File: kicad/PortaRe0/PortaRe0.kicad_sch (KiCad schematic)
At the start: 0 parts

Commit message: Add project docs and complete BQ25895 schematic
- Add Claude/ folder (CONTEXT.md, PROGRESS.md, PROJECT_PLAN.md, chat_logs/)
- Add KiCad hierarchical sheets (power, usb_hub, keyboard, audio)
- Complete BQ25895 power sheet schematic
  - TS pin: REGN-R6(10kΩ)-TS-R7(10kΩ)-GND divider
  - BAT/SYS/PGND/PAD/SW/BTST/REGN/PMID/DSEL all connected
  - Decoupling caps on VBAT and VSYS

Co-Authored-By: Claude Sonnet 4.6 <noreply@anthropic.com>
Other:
- added sheet audio (audio.kicad_sch)
- added sheet keyboard (keyboard.kicad_sch)
- added sheet power (power.kicad_sch)
- added sheet usb_hub (usb_hub.kicad_sch)
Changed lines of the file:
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@@
 	(generator_version "9.0")
 	(paper "A4")
+	(sheet
+		(at 16.51 96.52)
+		(size 90.17 88.9)
+		(exclude_from_sim no)
+		(in_bom yes)
+		(on_board yes)
+		(dnp no)
+		(fields_autoplaced yes)
+		(stroke
+			(width 0.1524)
+			(type solid)
+		)
+		(fill
+			(color 0 0 0 0.0000)
+		)
+		(property "Sheetname" "keyboard"
+			(at 16.51 95.8084 0)
+			(effects
+				(font
+					(size 1.27 1.27)
+				)
+				(justify left bottom)
+			)
+		)
+		(property "Sheetfile" "keyboard.kicad_sch"
+			(at 16.51 186.0046 0)
+			(effects
+				(font
+					(size 1.27 1.27)
+				)
+				(justify left top)
+			)
+		)
+		(instances
+			(project "PortaRe0"
+				(path "/479aadc4-f9a0-4ec2-b000-6a17237038f1"
+					(page "4")
+				)
+			)
+		)
+	)
+	(sheet
+		(at 107.95 96.52)
+		(size 90.17 88.9)
+		(exclude_from_sim no)
+		(in_bom yes)
+		(on_board yes)
+		(dnp no)
+		(fields_autoplaced yes)
+		(stroke
+			(width 0.1524)
+			(type solid)
+		)
+		(fill
+			(color 0 0 0 0.0000)
+		)
+		(property "Sheetname" "audio"
+			(at 107.95 95.8084 0)
+			(effects
+				(font
+					(size 1.27 1.27)
+				)
+				(justify left bottom)
+			)
+		)
+		(property "Sheetfile" "audio.kicad_sch"
+			(at 107.95 186.0046 0)
+			(effects
+				(font
+					(size 1.27 1.27)
+				)
+				(justify left top)
+			)
+		)
+		(instances
+			(project "PortaRe0"
+				(path "/479aadc4-f9a0-4ec2-b000-6a17237038f1"
+					(page "5")
+				)
+			)
+		)
+	)
+	(sheet
+		(at 107.95 17.78)
+		(size 90.17 77.47)
+		(exclude_from_sim no)
+		(in_bom yes)
+		(on_board yes)
+		(dnp no)
+		(fields_autoplaced yes)
+		(stroke
+			(width 0.1524)
+			(type solid)
+		)
+		(fill
+			(color 0 0 0 0.0000)
+		)
+		(property "Sheetname" "usb_hub"
+			(at 107.95 17.0684 0)
+			(effects
+				(font
+					(size 1.27 1.27)
+				)
+				(justify left bottom)
+			)
+		)
+		(property "Sheetfile" "usb_hub.kicad_sch"
+			(at 107.95 95.8346 0)
+			(effects
+				(font
+					(size 1.27 1.27)
+				)
+				(justify left top)
+			)
+		)
+		(instances
+			(project "PortaRe0"
+				(path "/479aadc4-f9a0-4ec2-b000-6a17237038f1"
+					(page "3")
+				)
+			)
+		)
+	)
+	(sheet
+		(at 16.51 17.78)
+		(size 90.17 77.47)
+		(exclude_from_sim no)
+		(in_bom yes)
+		(on_board yes)
+		(dnp no)
+		(fields_autoplaced yes)
+		(stroke
+			(width 0.1524)
+			(type solid)
+		)
+		(fill
+			(color 0 0 0 0.0000)
+		)
+		(property "Sheetname" "power"
+			(at 16.51 17.0684 0)
+			(effects
+				(font
+					(size 1.27 1.27)
+				)
+				(justify left bottom)
+			)
+		)
+		(property "Sheetfile" "power.kicad_sch"
+			(at 16.51 95.8346 0)
+			(effects
+				(font
+					(size 1.27 1.27)
+				)
+				(justify left top)
+			)
+		)
+		(instances
+			(project "PortaRe0"
+				(path "/479aadc4-f9a0-4ec2-b000-6a17237038f1"
+					(page "2")
+				)
+			)
+		)
+	)
 	(sheet_instances
 		(path "/"

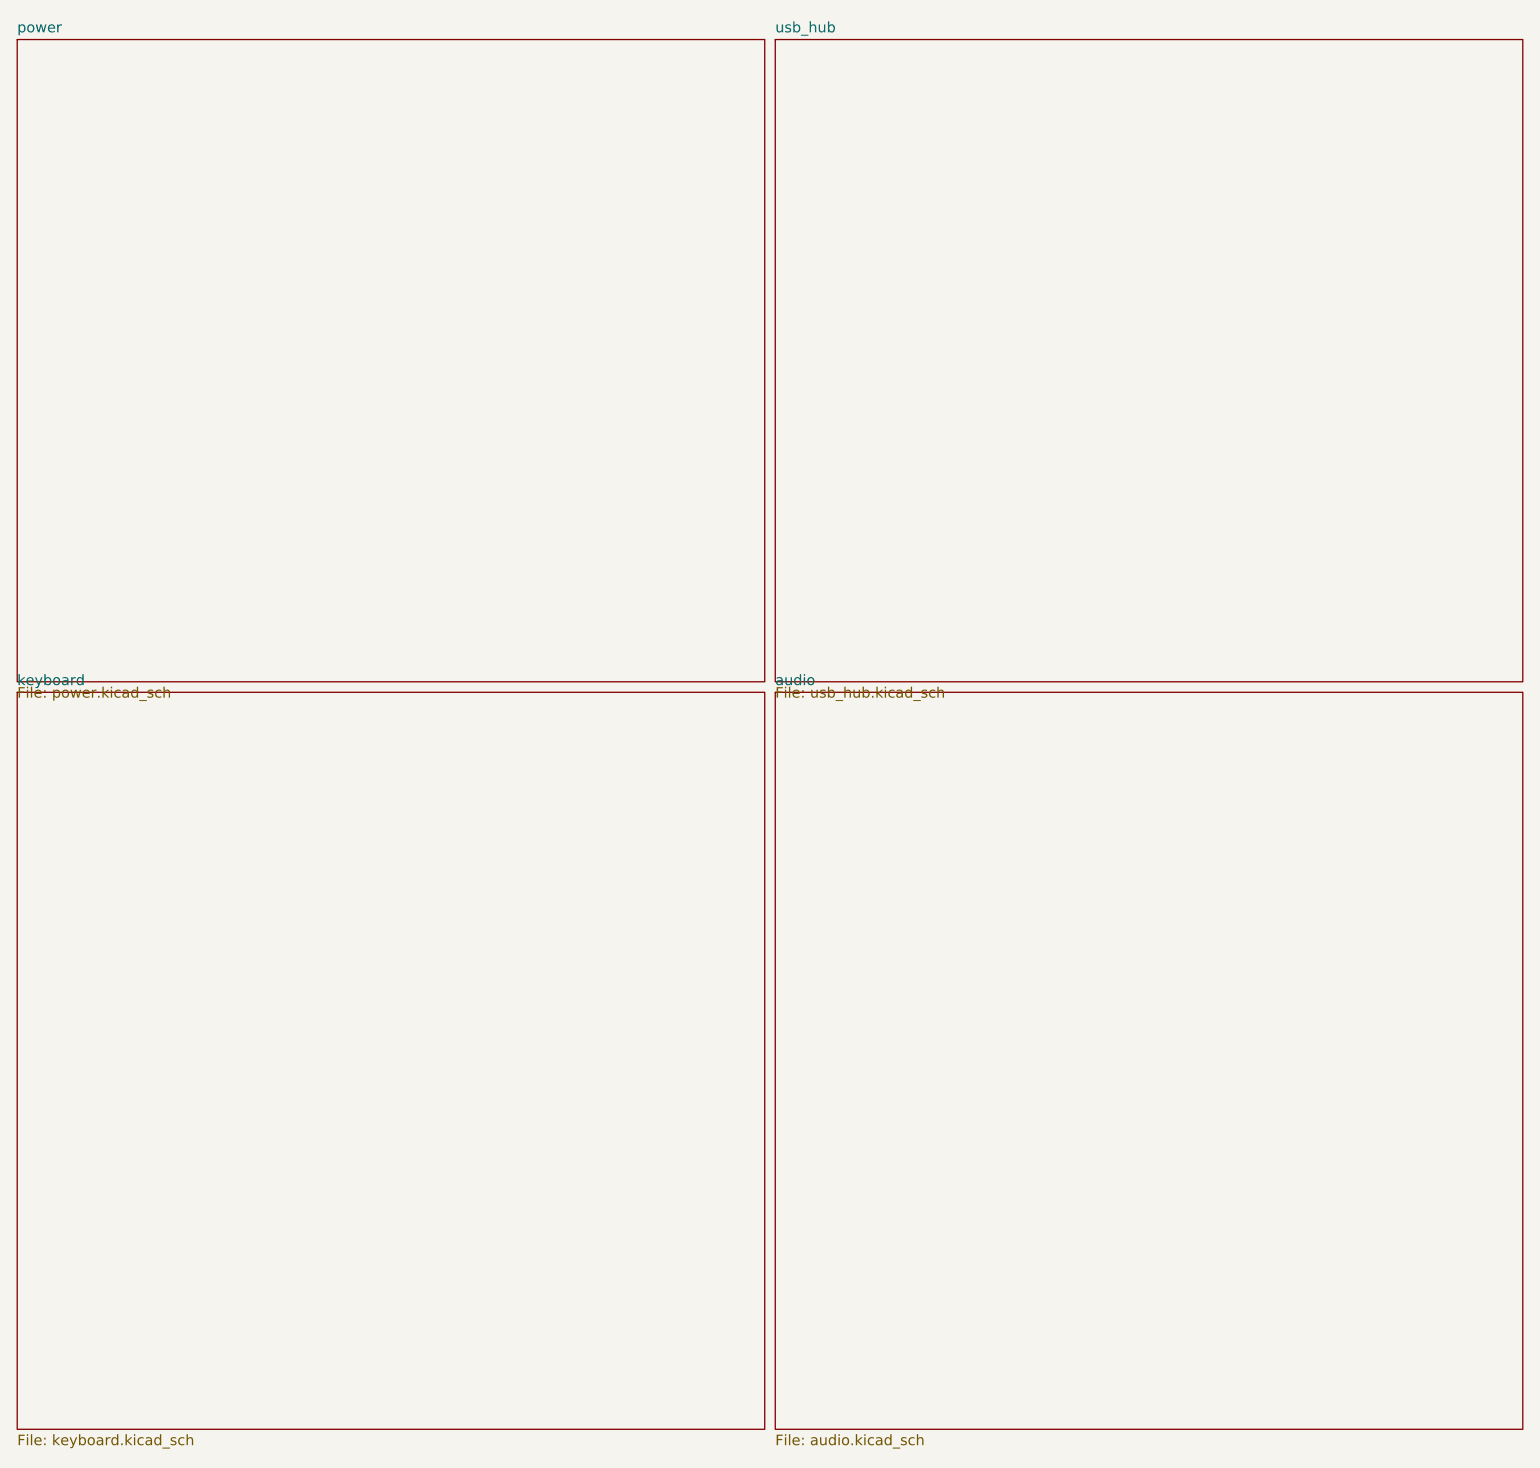
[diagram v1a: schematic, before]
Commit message: session07: キーレイアウト確定・GPIO割り当て・power回路レビュー
- キーレイアウト確定（66キー / 9×8マトリクス）、keyboard-layout.json追加
- RP2040 GPIO割り当て確定（29本/30本）をPROJECT_PLANに追記
- power回路レビュー（5V_SYS→パワーシンボル化、SCL/SDA/USB_DP/USB_DM→GlobalLabel）
- .gitignoreに.claude/を追加

Co-Authored-By: Claude Sonnet 4.6 <noreply@anthropic.com>
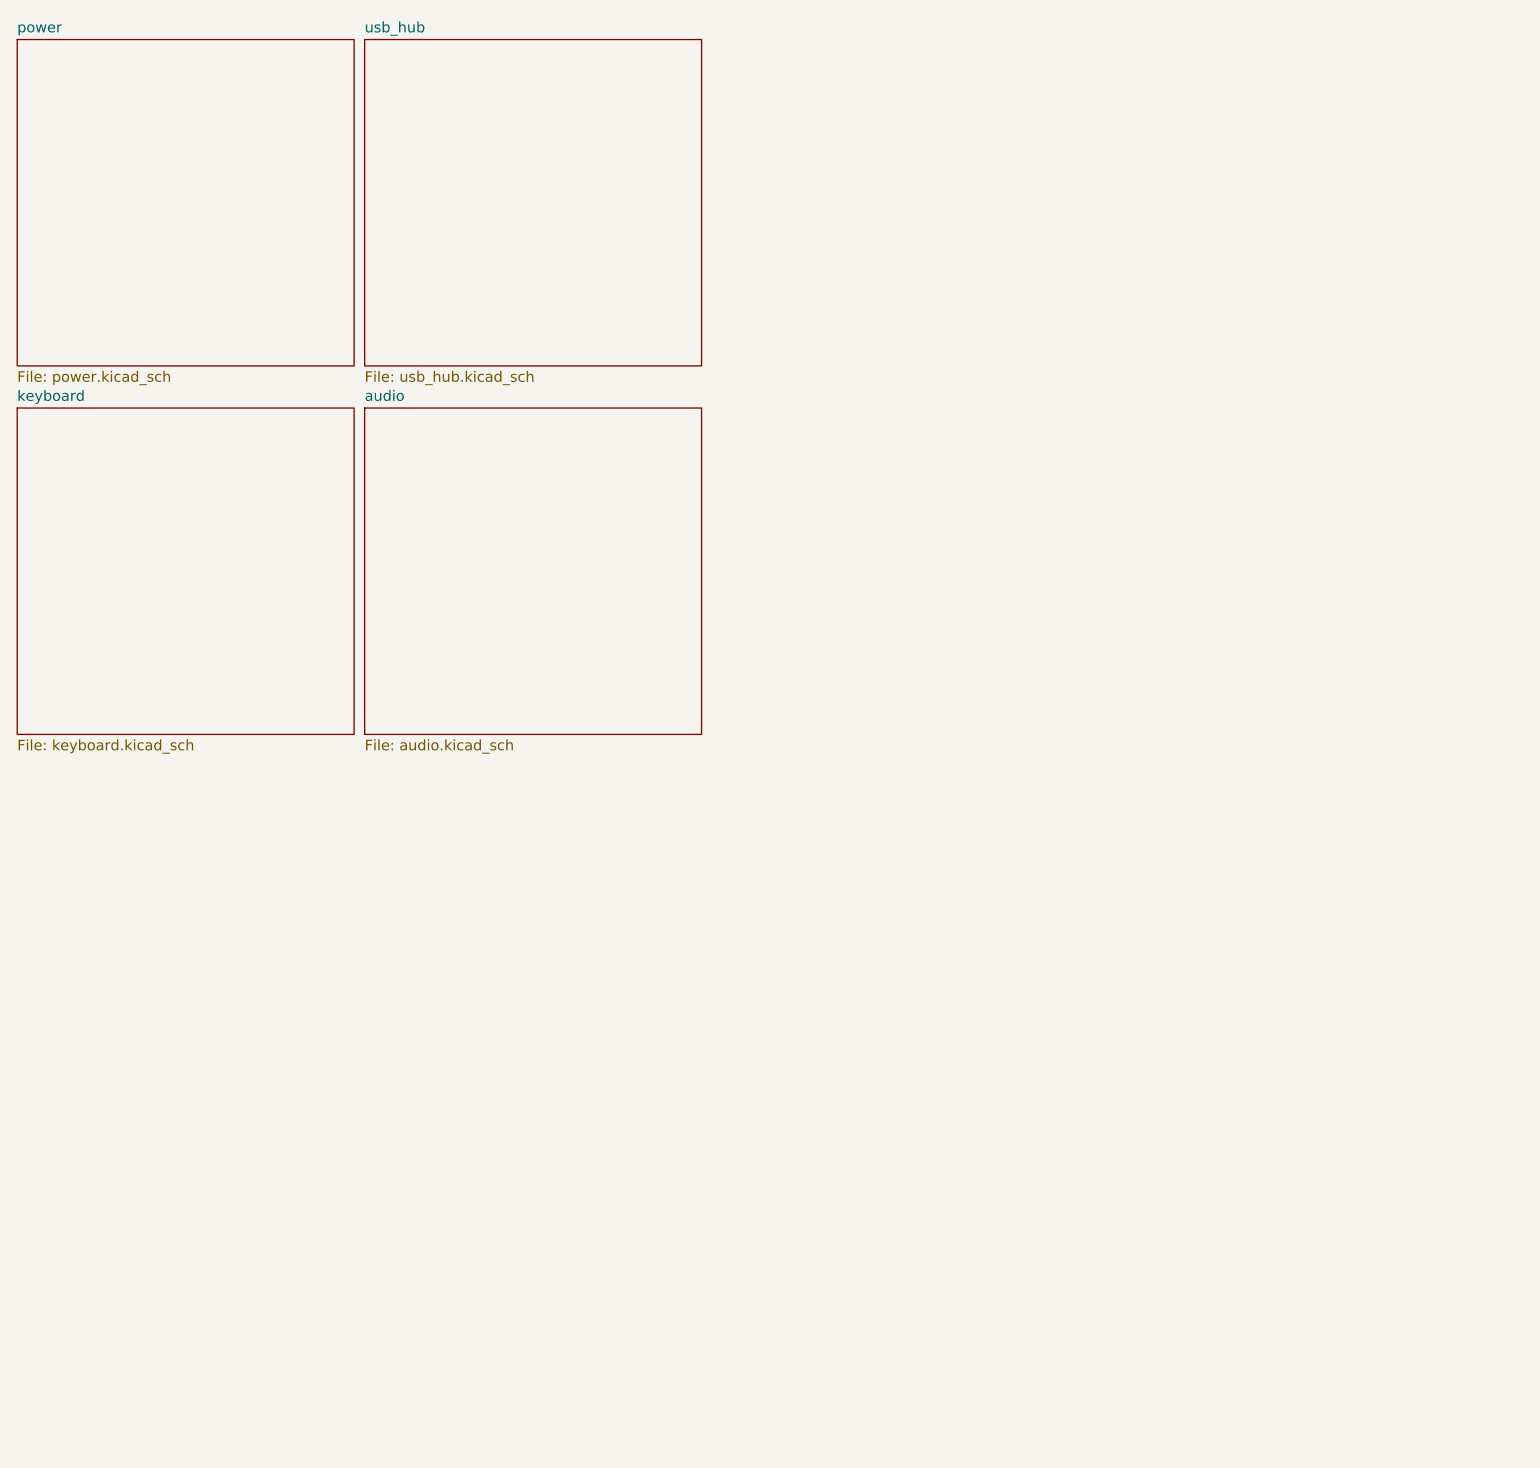
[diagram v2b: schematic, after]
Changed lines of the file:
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@@
 	(paper "A4")
 	(sheet
-		(at 16.51 96.52)
-		(size 90.17 88.9)
+		(at 16.51 62.23)
+		(size 40.64 39.37)
 		(exclude_from_sim no)
 		(in_bom yes)
@@
 		)
 		(property "Sheetname" "keyboard"
-			(at 16.51 95.8084 0)
+			(at 16.51 61.5184 0)
 			(effects
 				(font
@@
 		)
 		(property "Sheetfile" "keyboard.kicad_sch"
-			(at 16.51 186.0046 0)
+			(at 16.51 102.1846 0)
 			(effects
 				(font
@@
 	)
 	(sheet
-		(at 107.95 96.52)
-		(size 90.17 88.9)
+		(at 58.42 62.23)
+		(size 40.64 39.37)
 		(exclude_from_sim no)
 		(in_bom yes)
@@
 		)
 		(property "Sheetname" "audio"
-			(at 107.95 95.8084 0)
+			(at 58.42 61.5184 0)
 			(effects
 				(font
@@
 		)
 		(property "Sheetfile" "audio.kicad_sch"
-			(at 107.95 186.0046 0)
+			(at 58.42 102.1846 0)
 			(effects
 				(font
@@
 	)
 	(sheet
-		(at 107.95 17.78)
-		(size 90.17 77.47)
+		(at 58.42 17.78)
+		(size 40.64 39.37)
 		(exclude_from_sim no)
 		(in_bom yes)
@@
 		)
 		(property "Sheetname" "usb_hub"
-			(at 107.95 17.0684 0)
+			(at 58.42 17.0684 0)
 			(effects
 				(font
@@
 		)
 		(property "Sheetfile" "usb_hub.kicad_sch"
-			(at 107.95 95.8346 0)
+			(at 58.42 57.7346 0)
 			(effects
 				(font
@@
 	(sheet
 		(at 16.51 17.78)
-		(size 90.17 77.47)
+		(size 40.64 39.37)
 		(exclude_from_sim no)
 		(in_bom yes)
@@
 		)
 		(property "Sheetfile" "power.kicad_sch"
-			(at 16.51 95.8346 0)
+			(at 16.51 57.7346 0)
 			(effects
 				(font

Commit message: Docs: session18終了処理・PROGRESS/index更新・connectorsシート設計方針確定
- J_HDMI_CTRL: 24pin FPC 0.5mm (C2856805) ライブラリ取得・配置方針確定
- SBC接続: サブ基板→FPCに変更・スティフナーにMicro HDMIオス+USB-Cオス直付け方針
- connectors.kicad_sch 追加

Co-Authored-By: Claude Sonnet 4.6 <noreply@anthropic.com>
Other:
- added sheet Connectors (Connectors.kicad_sch)
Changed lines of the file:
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@@
 	(paper "A4")
+	(sheet
+		(at 101.6 17.78)
+		(size 39.37 39.37)
+		(exclude_from_sim no)
+		(in_bom yes)
+		(on_board yes)
+		(dnp no)
+		(fields_autoplaced yes)
+		(stroke
+			(width 0.1524)
+			(type solid)
+		)
+		(fill
+			(color 0 0 0 0.0000)
+		)
+		(property "Sheetname" "Connectors"
+			(at 101.6 17.0684 0)
+			(effects
+				(font
+					(size 1.27 1.27)
+				)
+				(justify left bottom)
+			)
+		)
+		(property "Sheetfile" "Connectors.kicad_sch"
+			(at 101.6 57.7346 0)
+			(effects
+				(font
+					(size 1.27 1.27)
+				)
+				(justify left top)
+			)
+		)
+		(instances
+			(project "PortaRe0"
+				(path "/479aadc4-f9a0-4ec2-b000-6a17237038f1"
+					(page "7")
+				)
+			)
+		)
+	)
 	(sheet
 		(at 16.51 62.23)

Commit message: Docs: session21終了処理・PROGRESS/index更新・connectorsシート完成・ERC対処
- connectors シート完成（J_SBC_HDMI / J_FAN配置完了）
- hdmi_adapter シート新設（別基板 / J_MICROHDMI Conn_02x08 + C2856805）
- J_FAN: F16FB選定（16×16×4.5mm 5V）/ BSS138回路 / FAN_PWM GlobalLabel
- 全シートERC実施・対処完了（VL812未接続ピン / SWD NC / DC10FB追加等）

Co-Authored-By: Claude Sonnet 4.6 <noreply@anthropic.com>
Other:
- added sheet hdmi_adapter (hdmi_adapter.kicad_sch)
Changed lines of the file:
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@@
 	(paper "A4")
+	(sheet
+		(at 101.6 62.23)
+		(size 39.37 39.37)
+		(exclude_from_sim no)
+		(in_bom yes)
+		(on_board yes)
+		(dnp no)
+		(fields_autoplaced yes)
+		(stroke
+			(width 0.1524)
+			(type solid)
+		)
+		(fill
+			(color 0 0 0 0.0000)
+		)
+		(property "Sheetname" "hdmi_adapter"
+			(at 101.6 61.5184 0)
+			(effects
+				(font
+					(size 1.27 1.27)
+				)
+				(justify left bottom)
+			)
+		)
+		(property "Sheetfile" "hdmi_adapter.kicad_sch"
+			(at 101.6 102.1846 0)
+			(effects
+				(font
+					(size 1.27 1.27)
+				)
+				(justify left top)
+			)
+		)
+		(instances
+			(project "PortaRe0"
+				(path "/479aadc4-f9a0-4ec2-b000-6a17237038f1"
+					(page "7")
+				)
+			)
+		)
+	)
 	(sheet
 		(at 101.6 17.78)
@@
 			(project "PortaRe0"
 				(path "/479aadc4-f9a0-4ec2-b000-6a17237038f1"
-					(page "7")
+					(page "6")
 				)
 			)

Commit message: KiCad: usb_adapterシート新設・connectorsシート整理
- usb_adapter.kicad_sch 新設（J_SBC_USB1/J_SBC_USB2を移動）
- FPCテール直挿し方式採用（中間コネクタなし）
- FPC 24pin ピン割り当て確定（差動ペア間GND配置）
- connectorsシートにC2856805（ZIF）×2追加
- .gitignore: kicad/PDF/ を除外に追加

Co-Authored-By: Claude Sonnet 4.6 <noreply@anthropic.com>
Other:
- added sheet usb_adapter (usb_adapter.kicad_sch)
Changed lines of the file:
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@@
+		)
+	)
+	(sheet
+		(at 16.51 106.68)
+		(size 40.64 39.37)
+		(exclude_from_sim no)
+		(in_bom yes)
+		(on_board yes)
+		(dnp no)
+		(fields_autoplaced yes)
+		(stroke
+			(width 0.1524)
+			(type solid)
+		)
+		(fill
+			(color 0 0 0 0.0000)
+		)
+		(property "Sheetname" "usb_adapter"
+			(at 16.51 105.9684 0)
+			(effects
+				(font
+					(size 1.27 1.27)
+				)
+				(justify left bottom)
+			)
+		)
+		(property "Sheetfile" "usb_adapter.kicad_sch"
+			(at 16.51 146.6346 0)
+			(effects
+				(font
+					(size 1.27 1.27)
+				)
+				(justify left top)
+			)
+		)
+		(instances
+			(project "PortaRe0"
+				(path "/479aadc4-f9a0-4ec2-b000-6a17237038f1"
+					(page "8")
+				)
+			)
 		)
 	)

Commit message: Docs/KiCad: session31終了処理・PROGRESS/index更新
- キルスイッチ確定: MSK12C02(C431540) EN制御方式・KiCad配線完了
- ヘッドフォンジャック確定: PJ-307C(C16684) TH / 配線・pull-up完了
- J4バッテリーコネクタ: S8B-PH-K-S-LF-SN(C157915) 水平型確定
- BOM Y4フットプリント修正
- 新規ライブラリ追加: MSK12C02/PJ-307C/S8B-PH-K-S他
- Phase 2 回路設計 全シート完了

Co-Authored-By: Claude Sonnet 4.6 <noreply@anthropic.com>
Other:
- added sheet m2_ssd (m2_ssd.kicad_sch)
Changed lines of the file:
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@@
+	)
+	(sheet
+		(at 58.42 106.68)
+		(size 40.64 39.37)
+		(exclude_from_sim no)
+		(in_bom yes)
+		(on_board yes)
+		(dnp no)
+		(fields_autoplaced yes)
+		(stroke
+			(width 0.1524)
+			(type solid)
+		)
+		(fill
+			(color 0 0 0 0.0000)
+		)
+		(property "Sheetname" "m2_ssd"
+			(at 58.42 105.9684 0)
+			(effects
+				(font
+					(size 1.27 1.27)
+				)
+				(justify left bottom)
+			)
+		)
+		(property "Sheetfile" "m2_ssd.kicad_sch"
+			(at 58.42 146.6346 0)
+			(effects
+				(font
+					(size 1.27 1.27)
+				)
+				(justify left top)
+			)
+		)
+		(instances
+			(project "PortaRe0"
+				(path "/479aadc4-f9a0-4ec2-b000-6a17237038f1"
+					(page "9")
+				)
+			)
+		)
 	)
 	(sheet
